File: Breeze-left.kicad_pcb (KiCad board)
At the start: 2 copper layers, 149.6 x 114.9 mm, 72 parts, among them SW1 CHOCXHSPCB-1U, SW10 CHOCXHSPCB-1U, SW11 CHOCXHSPCB-1U, SW12 CHOCXHSPCB-1U, SW13 CHOCXHSPCB-1U, SW14 CHOCXHSPCB-1U, SW15 CHOCXHSPCB-1U, SW16 CHOCXHSPCB-1U, SW17 CHOCXHSPCB-1U, SW18 CHOCXHSPCB-1U, SW19 CHOCXHSPCB-1U, SW2 CHOCXHSPCB-1U, SW20 CHOCXHSPCB-1U, SW21 CHOCXHSPCB-1U, SW22 CHOCXHSPCB-1U, SW23 CHOCXHSPCB-1U, SW24 CHOCXHSPCB-1U, SW3 CHOCXHSPCB-1U, SW4 CHOCXHSPCB-1U, SW5 CHOCXHSPCB-1U, SW6 CHOCXHSPCB-1U, SW7 CHOCXHSPCB-1U, SW8 CHOCXHSPCB-1U, SW9 CHOCXHSPCB-1U

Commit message: do left
use gitignore
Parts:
- removed BATT_CONN1: ~, Breeze:BATT_PADS
- removed H18, H19: M3-HOLE, Breeze:M3-HOLE
- added H1: MountingHole_M3, MountingHole:MountingHole_3.2mm_M3_ISO14580_Pad_TopOnly, F.Cu at (179.5, 120.0)
- added H10: MountingHole_M3, MountingHole:MountingHole_3.2mm_M3_ISO14580_Pad_TopOnly, F.Cu at (269.2, 179.6)
- added J1: Conn_01x02, Breeze:BATT_PADS, F.Cu at (297.5, 170.5)
- D1, D10, D11, D12, D13, D14, D15, D16, D17, D18, D19, D2, D20, D21, D22, D23, D24, D3, D4, D5, D6, D7, D8, D9: value DIODE -> 1N4007W; footprint Breeze:SOD-123FL -> Breeze:SOD-123FL_L2.7-W1.8-LS3.7-RD
- D25: renamed from DTC1; value DIODE -> 1N4007W; footprint Breeze:SOD-123FL -> Breeze:SOD-123FL_L2.7-W1.8-LS3.7-RD
- D26: renamed from DTC2; value DIODE -> 1N4007W; footprint Breeze:SOD-123FL -> Breeze:SOD-123FL_L2.7-W1.8-LS3.7-RD
- D27: renamed from DTC3; value DIODE -> 1N4007W; footprint Breeze:SOD-123FL -> Breeze:SOD-123FL_L2.7-W1.8-LS3.7-RD
- D28: renamed from DTC4; value DIODE -> 1N4007W; footprint Breeze:SOD-123FL -> Breeze:SOD-123FL_L2.7-W1.8-LS3.7-RD
- H2, H3, H4, H5, H6, H7, H8, H9: value M3-HOLE -> MountingHole_M3; footprint Breeze:M3-HOLE -> MountingHole:MountingHole_3.2mm_M3_ISO14580_Pad_TopOnly; moved to F.Cu
- moved H2 79.6 mm to (179.5, 139.1), turned to 0 degrees
- moved H4 58.1 mm to (217.7, 114.4), turned to 0 degrees
- moved H7 38.3 mm to (255.7, 116.2), turned to 0 degrees
- moved H9 28.5 mm to (255.7, 154.5), turned to 0 degrees
- moved H3 19.1 mm to (179.5, 158.2), turned to 0 degrees
- moved D21 9.05 mm to (217.0, 159.9)
- moved D19 8.25 mm to (255.0, 165.5)
- moved D15 5.78 mm to (217.0, 140.7)
- moved D3 5.68 mm to (217.0, 102.7)
- moved D11 5.66 mm to (178.8, 128.9)
- moved D9 5.63 mm to (217.0, 121.8)
- moved D17 5.61 mm to (178.7, 148.0)
- moved D5 5.32 mm to (178.8, 109.9)
- moved D26 4.63 mm to (245.5, 186.2)
- moved D13 4.23 mm to (255.0, 145.5)
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- renumbered LGO1 to G1, STABL1 to H11, PWR1 to SW1, RST1 to SW2, MCU-MAIN1 to U1, SW1 to XS1, SW10 to XS10, SW11 to XS11, SW12 to XS12, SW13 to XS13, SW14 to XS14, SW15 to XS15, SW16 to XS16, SW17 to XS17, SW18 to XS18, SW19 to XS19, SW2 to XS2, SW20 to XS20, SW21 to XS21, SW22 to XS22, SW23 to XS23, SW24 to XS24, TC1 to XS25, TC2 to XS26, TC3 to XS27, TC4 to XS28, SW3 to XS3, SW4 to XS4, SW5 to XS5, SW6 to XS6, SW7 to XS7, SW8 to XS8, SW9 to XS9
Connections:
- net BAT_PLUS renamed +BATT
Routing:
- net ROW3: track 163.6 -> 174.3 mm
- net ROW1: track 136.0 -> 143.0 mm
- net ROW0: track 149.0 -> 155.8 mm
- net ROW2: track 150.3 -> 157.0 mm
- net COL5: track 209.8 -> 213.3 mm
- net Net-(D8-A): track 9.71 -> 12.9 mm
- net Net-(D18-A): track 9.72 -> 12.9 mm
- net Net-(D14-A): track 9.73 -> 12.9 mm
- net ROW4: track 103.8 -> 106.8 mm
- net Net-(D22-A): track 9.73 -> 12.6 mm
- net Net-(D12-A): track 9.72 -> 12.6 mm
- net Net-(D16-A): track 9.73 -> 12.5 mm
- net Net-(D4-A): track 9.73 -> 12.5 mm
- net Net-(D10-A): track 9.96 -> 12.5 mm
- net Net-(D2-A): track 9.73 -> 12.3 mm
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
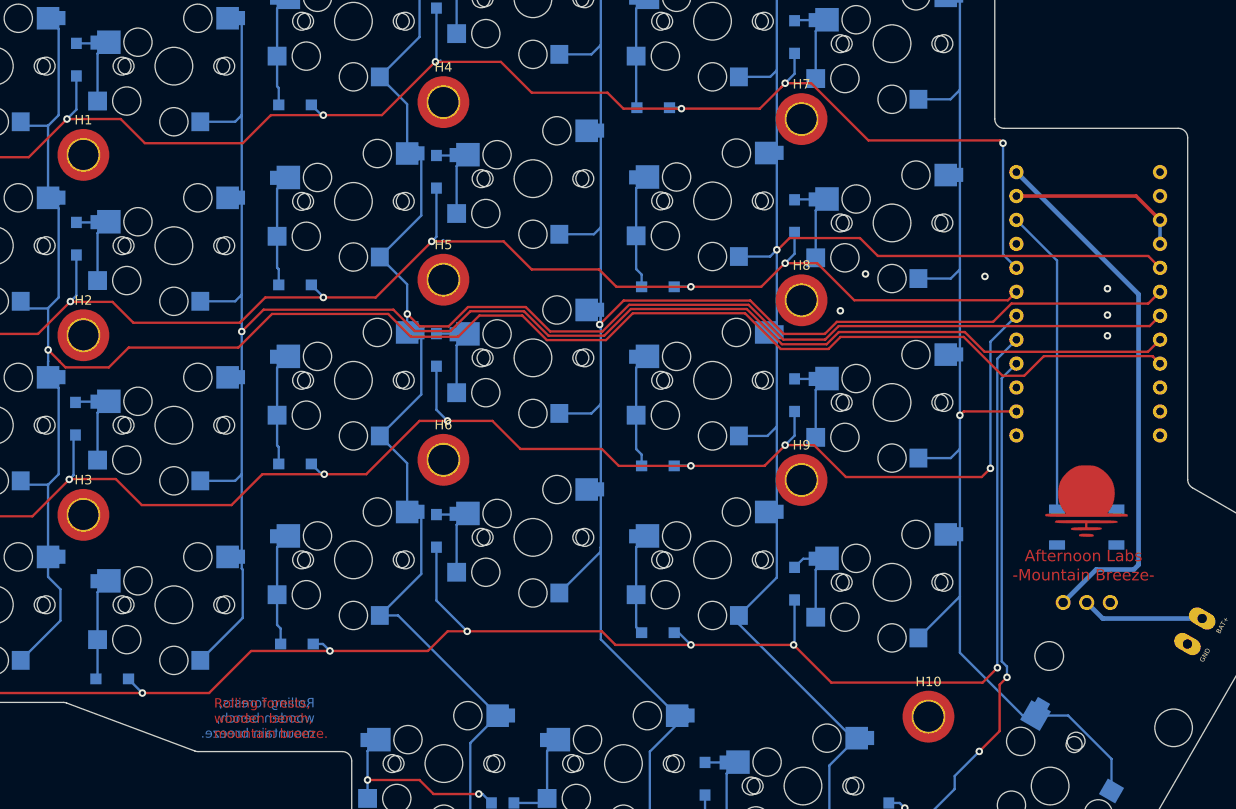
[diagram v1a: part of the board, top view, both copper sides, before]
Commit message: redo left PCB, redraw supermini symbol
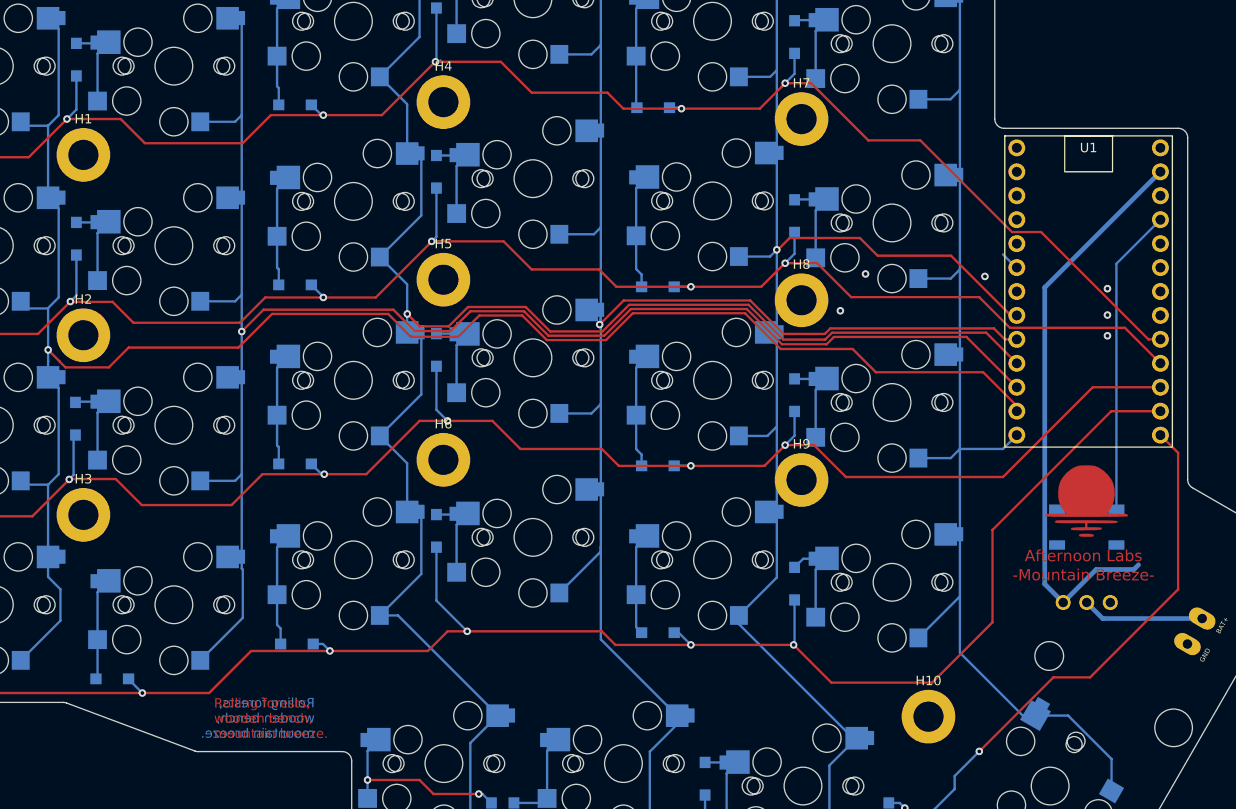
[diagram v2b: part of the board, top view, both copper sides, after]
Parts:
- H1, H10, H2, H3, H4, H5, H6, H7, H8, H9: footprint MountingHole:MountingHole_3.2mm_M3_ISO14580_Pad_TopOnly -> MountingHole:MountingHole_3.2mm_M3_ISO7380_Pad
- U1: value PRO-MICRO -> NRF Supermini; footprint Breeze:ProMicro_1-Sided -> Breeze:NRF_Supermini
- moved U1 1.30 mm to (286.2, 134.5)
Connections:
- U1 pad 1: unconnected-(U1-TX(PD3)-Pad1) -> GND
- U1 pad 10: unconnected-(U1-D7(PE6)-Pad10) -> COL3
- U1 pad 11: unconnected-(U1-D8(PB4)-Pad11) -> COL4
- U1 pad 12: unconnected-(U1-D9(PB5)-Pad12) -> COL5
- U1 pad 13: unconnected-(U1-D10(PB6)-Pad13) -> COL0
- U1 pad 14: COL0 -> ROW4
- U1 pad 16: ROW4 -> ROW2
- U1 pad 17: ROW3 -> ROW1
- U1 pad 18: ROW2 -> ROW0
- U1 pad 19: ROW1 -> unconnected-(U1-D19(0.02)-Pad19)
- U1 pad 20: ROW0 -> unconnected-(U1-D20(0.29)-Pad20)
- U1 pad 21: VCC -> unconnected-(U1-D21(0.31)-Pad21)
- U1 pad 22: RST -> VCC
- U1 pad 23: GND -> RST
- U1 pad 24: +BATT -> GND
- U1 pad 3: GND -> unconnected-(U1-D0(0.08)-Pad3)
- U1 pad 5: COL1 -> GND
- U1 pad 6: COL2 -> unconnected-(U1-D2(0.17)-Pad6)
- U1 pad 7: COL3 -> unconnected-(U1-D3(0.20)-Pad7)
- U1 pad 8: COL4 -> COL1
- U1 pad 9: COL5 -> COL2
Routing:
- net GND: track 19.0 -> 0.12 mm
- net ROW1: track 143.0 -> 160.6 mm
- net COL2: track 182.7 -> 166.4 mm
- net COL5: track 213.3 -> 197.6 mm
- net COL4: track 190.1 -> 175.5 mm
- net COL3: track 194.8 -> 180.2 mm
- net COL1: track 156.5 -> 143.4 mm
- net ROW0: track 155.8 -> 167.3 mm, vias 7 -> 6
- net +BATT: track 56.7 -> 61.2 mm
- net ROW2: track 157.0 -> 161.3 mm, vias 7 -> 6
- net ROW4: track 106.8 -> 108.9 mm, vias 2 -> 1
- net unconnected-(U1-D2(0.17)-Pad6): track 0.00 -> 2.01 mm
- net ROW3: track 174.3 -> 172.9 mm, vias 7 -> 6
- net COL0: track 120.7 -> 121.2 mm, vias 1 -> 0

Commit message: done
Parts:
- moved D27 1.28 mm to (226.5, 190.5)
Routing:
- net Net-(D27-A): track 11.7 -> 10.4 mm
- net COL1: track 143.4 -> 144.0 mm

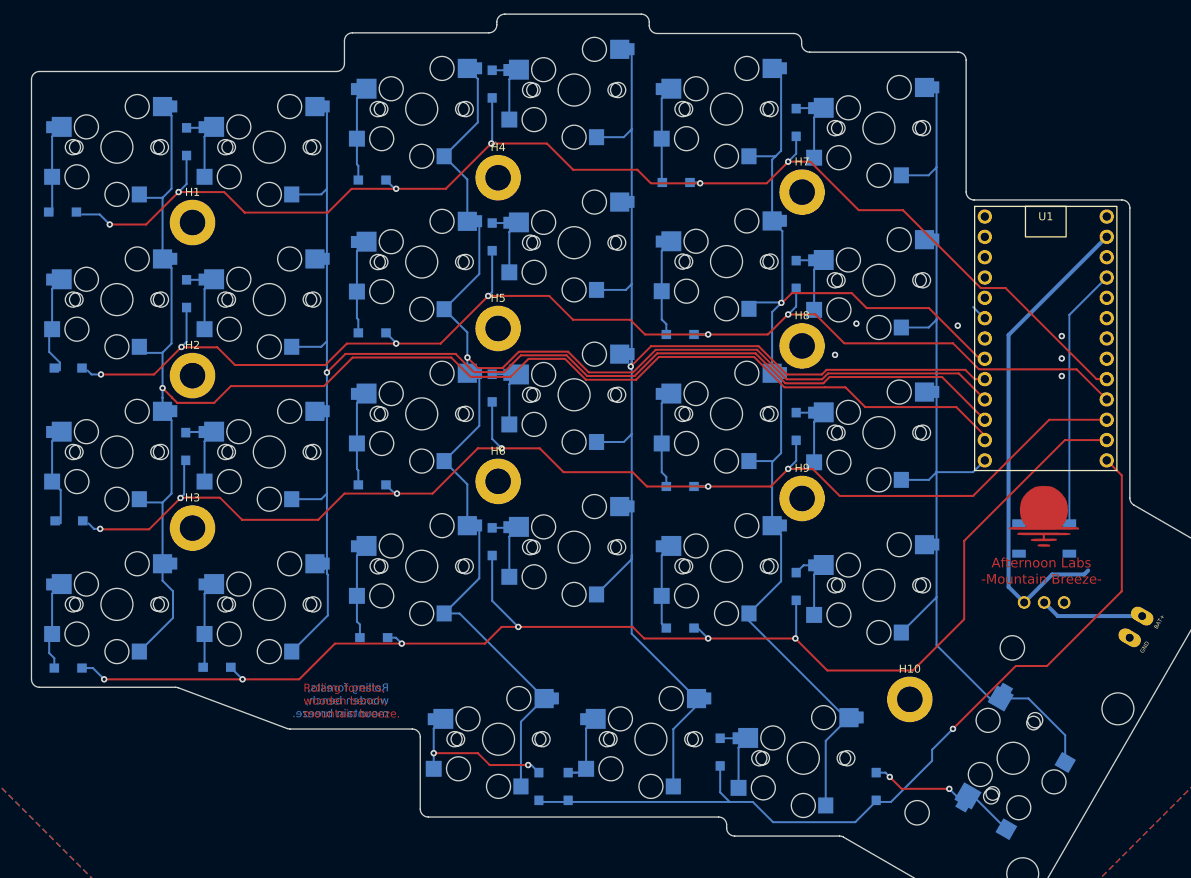
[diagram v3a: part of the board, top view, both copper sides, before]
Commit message: trace width parity, correct arduino mounting side
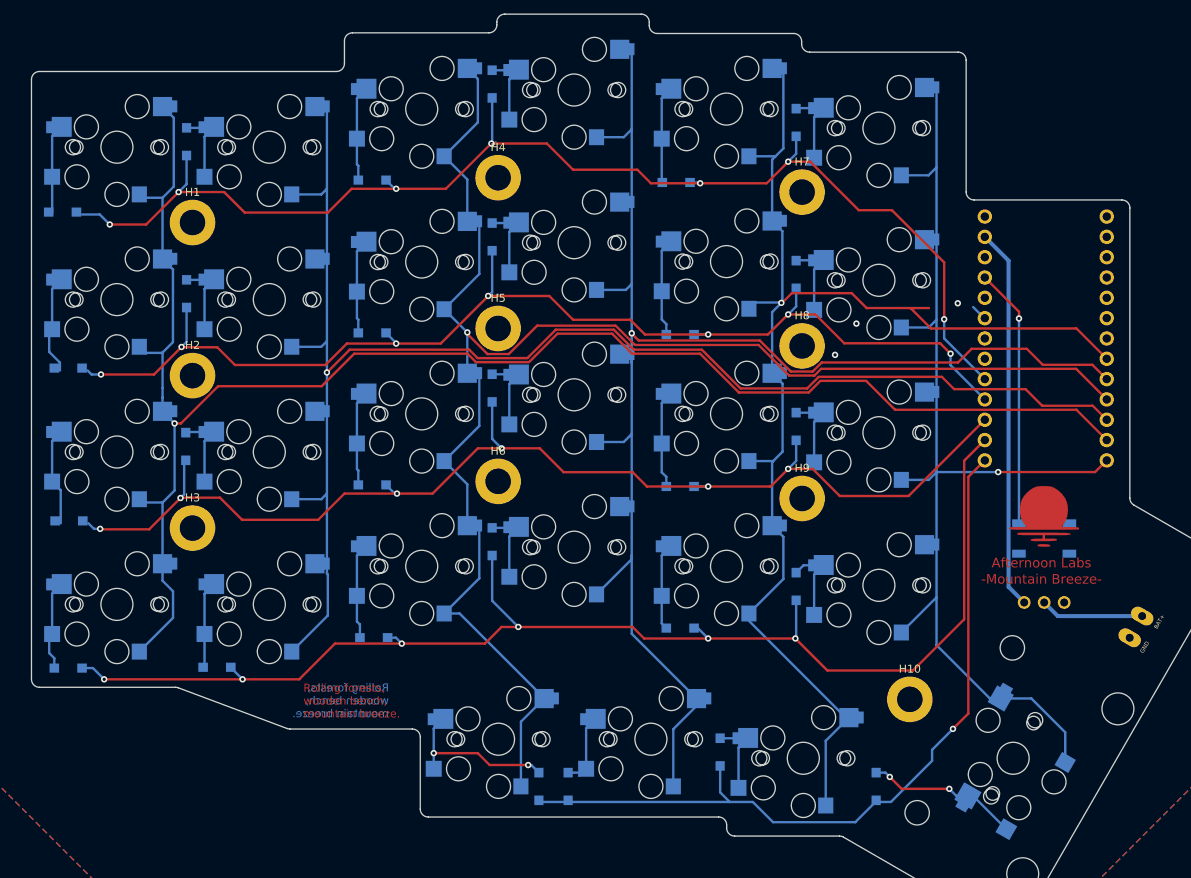
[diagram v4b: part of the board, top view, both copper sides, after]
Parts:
- U1: moved to B.Cu
- turned U1 to 180 degrees
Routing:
- net COL1: track 144.0 -> 161.9 mm
- net COL2: track 166.4 -> 182.9 mm
- net COL3: track 180.2 -> 195.8 mm
- net COL0: track 121.2 -> 136.6 mm, vias 0 -> 1
- net ROW2: track 161.3 -> 146.1 mm
- net COL4: track 175.5 -> 190.6 mm
- net COL5: track 197.6 -> 212.5 mm
- net ROW1: track 160.6 -> 146.3 mm, vias 6 -> 7
- net +BATT: track 61.2 -> 47.7 mm
- net ROW4: track 108.9 -> 98.7 mm
- net ROW0: track 167.3 -> 157.6 mm, vias 6 -> 7
- net ROW3: track 172.9 -> 163.6 mm
- net unconnected-(U1-D21(0.31)-Pad21): track 0.00 -> 2.01 mm
- net unconnected-(U1-D2(0.17)-Pad6): track 2.01 -> 0.00 mm
- net unconnected-(U1-D19(0.02)-Pad19): track 0.00 -> 0.64 mm
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
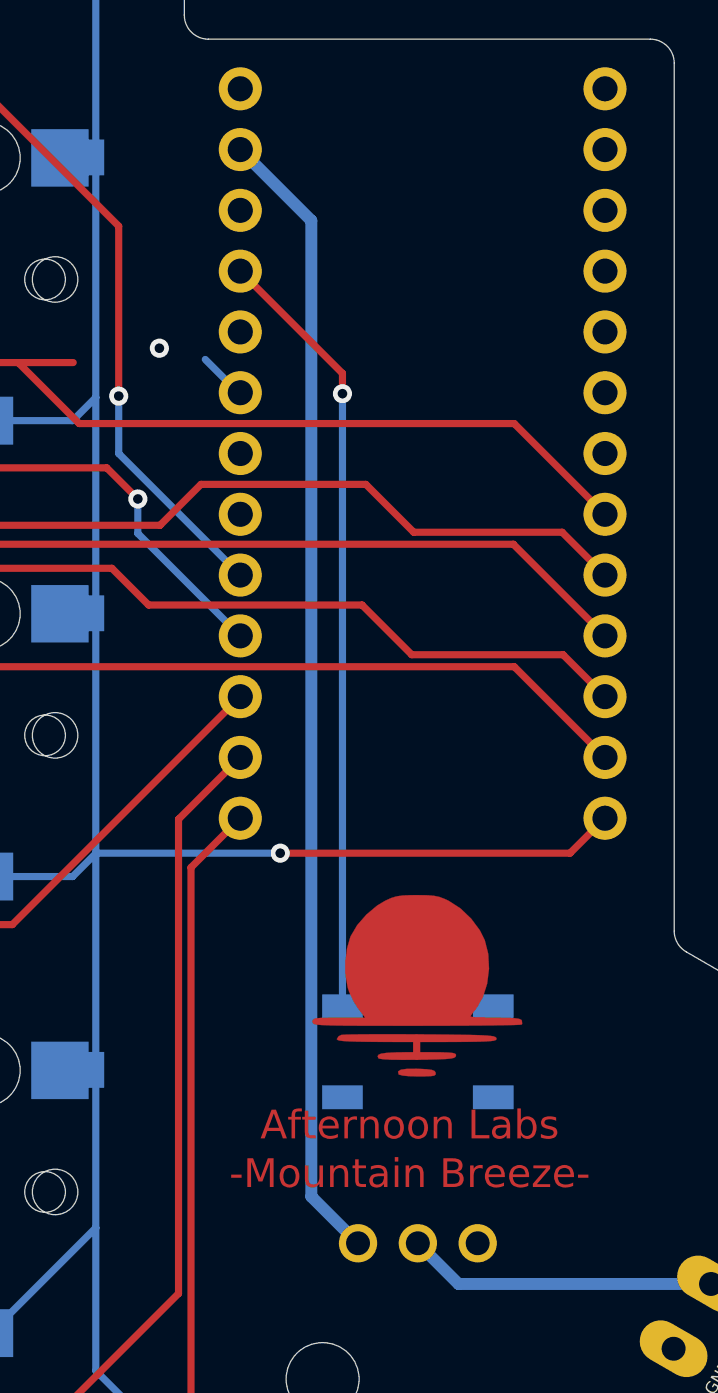
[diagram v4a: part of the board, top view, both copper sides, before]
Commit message: fix mis-named component(xs25)
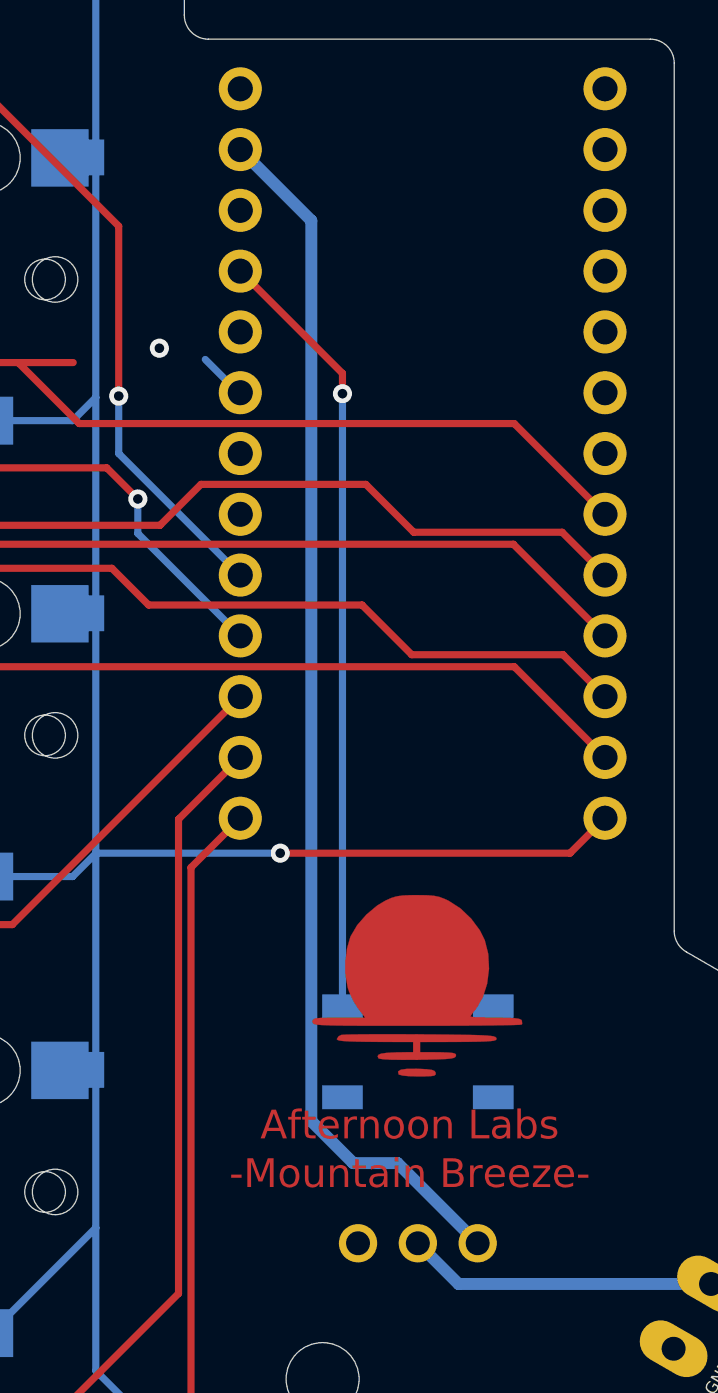
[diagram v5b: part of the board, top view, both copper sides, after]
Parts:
- turned SW1 to 180 degrees
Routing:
- net +BATT: track 47.7 -> 50.9 mm
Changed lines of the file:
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@@
 	(footprint "Breeze:SS12D00"
 		(layer "B.Cu")
-		(at 286 167.5)
+		(at 286 167.5 180)
 		(property "Reference" "SW1"
-			(at 0 -2.7 180)
+			(at 0 -2.7 0)
 			(layer "B.SilkS")
 			(effects
@@
 		)
 		(property "Value" "SW_SPDT"
-			(at 0 1.5 180)
+			(at 0 1.5 0)
 			(layer "B.Fab")
 			(hide yes)
@@
 		)
 		(property "Datasheet" "~"
-			(at 0 0 180)
+			(at 0 0 0)
 			(layer "B.Fab")
 			(hide yes)
@@
 		)
 		(property "Description" "Switch, single pole double throw"
-			(at 0 0 180)
+			(at 0 0 0)
 			(layer "B.Fab")
 			(hide yes)
@@
 		)
 		(property "LCSC" "C145861"
-			(at 0 0 180)
+			(at 0 0 0)
 			(unlocked yes)
 			(layer "B.Fab")
@@
 		(attr through_hole)
 		(fp_line
-			(start -4.25 -1.75)
-			(end 4.25 -1.75)
+			(start 4.25 1.75)
+			(end -4.25 1.75)
 			(stroke
 				(width 0.1)
@@
 		)
 		(fp_line
-			(start -4.25 1.75)
-			(end -4.25 -1.75)
+			(start 4.25 -1.75)
+			(end 4.25 1.75)
 			(stroke
 				(width 0.1)
@@
 		)
 		(fp_line
-			(start 4.25 -1.75)
-			(end 4.25 1.75)
+			(start -4.25 1.75)
+			(end -4.25 -1.75)
 			(stroke
 				(width 0.1)
@@
 		)
 		(fp_line
-			(start 4.25 1.75)
-			(end -4.25 1.75)
+			(start -4.25 -1.75)
+			(end 4.25 -1.75)
 			(stroke
 				(width 0.1)
@@
 		)
 		(pad "1" thru_hole circle
-			(at -2.5 0)
+			(at -2.5 0 180)
 			(size 1.6 1.6)
 			(drill 1)
@@
 		)
 		(pad "2" thru_hole circle
-			(at 0 0)
+			(at 0 0 180)
 			(size 1.6 1.6)
 			(drill 1)
@@
 		)
 		(pad "3" thru_hole circle
-			(at 2.5 0)
+			(at 2.5 0 180)
 			(size 1.6 1.6)
 			(drill 1)
@@
 	)
 	(segment
-		(start 283.5 167.5)
-		(end 281.549 165.549)
+		(start 281.549 162.399)
+		(end 283.3 164.15)
+		(width 0.5)
+		(layer "B.Cu")
+		(net 44)
+	)
+	(segment
+		(start 281.549 124.769)
+		(end 281.549 162.399)
+		(width 0.5)
+		(layer "B.Cu")
+		(net 44)
+	)
+	(segment
+		(start 285.15 164.15)
+		(end 288.5 167.5)
 		(width 0.5)
 		(layer "B.Cu")
@@
 	)
 	(segment
-		(start 281.549 165.549)
+		(start 278.58 121.8)
 		(end 281.549 124.769)
 		(width 0.5)
@@
 	)
 	(segment
-		(start 281.549 124.769)
-		(end 278.58 121.8)
+		(start 283.3 164.15)
+		(end 285.15 164.15)
 		(width 0.5)
 		(layer "B.Cu")
